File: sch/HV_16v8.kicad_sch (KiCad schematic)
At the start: 14 parts, among them J5 STPR_OUT, J6 Conn_01x03_Socket, U7 DRV8461SPWP

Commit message: gah
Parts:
- C30: footprint Capacitor_SMD:CP_Elec_8x10 -> Capacitor_THT:CP_Radial_D8.0mm_P3.50mm
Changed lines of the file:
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@@
 			)
 		)
-		(property "Footprint" "Capacitor_SMD:CP_Elec_8x10"
+		(property "Footprint" "Capacitor_THT:CP_Radial_D8.0mm_P3.50mm"
 			(at 20.0152 30.48 0)
 			(hide yes)

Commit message: reroute
doooom
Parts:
- added C46: 1uF, Capacitor_SMD:C_0402_1005Metric, symbol Device:C_Small
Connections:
- net BOUT1: now also J5.4 (Pin_4); no longer J5.3 (Pin_3)
- net BOUT2: now also J5.3 (Pin_3); no longer J5.4 (Pin_4)
- net DVDD: now also C46.1
- net GND: now also C46.2
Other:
- moved on the sheet: C34
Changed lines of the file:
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@@
+	)
+	(junction
+		(at 82.55 45.72)
+		(diameter 0)
+		(color 0 0 0 0)
+	)
+	(junction
+		(at 92.71 39.37)
+		(diameter 0)
+		(color 0 0 0 0)
+	)
+	(junction
+		(at 41.91 30.48)
+		(diameter 0)
+		(color 0 0 0 0)
+	)
+	(junction
+		(at 104.14 39.37)
+		(diameter 0)
+		(color 0 0 0 0)
+	)
+	(junction
+		(at 104.14 44.45)
+		(diameter 0)
+		(color 0 0 0 0)
+	)
+	(junction
+		(at 63.5 55.88)
+		(diameter 0)
+		(color 0 0 0 0)
 	)
 	(junction
@@
 	)
 	(junction
-		(at 82.55 45.72)
+		(at 30.48 30.48)
 		(diameter 0)
 		(color 0 0 0 0)
 	)
 	(junction
-		(at 92.71 39.37)
+		(at 115.57 44.45)
 		(diameter 0)
 		(color 0 0 0 0)
 	)
 	(junction
-		(at 41.91 30.48)
-		(diameter 0)
-		(color 0 0 0 0)
-	)
-	(junction
-		(at 104.14 39.37)
-		(diameter 0)
-		(color 0 0 0 0)
-	)
-	(junction
-		(at 104.14 44.45)
-		(diameter 0)
-		(color 0 0 0 0)
-	)
-	(junction
-		(at 63.5 55.88)
+		(at 115.57 39.37)
 		(diameter 0)
 		(color 0 0 0 0)
@@
 		(color 0 0 0 0)
 	)
-	(junction
-		(at 30.48 30.48)
-		(diameter 0)
-		(color 0 0 0 0)
-	)
-	(junction
-		(at 115.57 44.45)
-		(diameter 0)
-		(color 0 0 0 0)
-	)
-	(junction
-		(at 115.57 39.37)
-		(diameter 0)
-		(color 0 0 0 0)
-	)
 	(wire
 		(pts
@@
 	(wire
 		(pts
+			(xy 19.05 20.32) (xy 19.05 22.86)
+		)
+		(stroke
+			(width 0)
+			(type default)
+		)
+	)
+	(wire
+		(pts
 			(xy 41.91 30.48) (xy 41.91 33.02)
 		)
@@
 	(wire
 		(pts
+			(xy 55.88 83.82) (xy 55.88 88.9)
+		)
+		(stroke
+			(width 0)
+			(type default)
+		)
+	)
+	(wire
+		(pts
 			(xy 64.77 83.82) (xy 69.85 83.82)
 		)
@@
 	)
 	(label "BOUT2"
-		(at 142.24 69.85 180)
+		(at 142.24 67.31 180)
 		(effects
 			(font
@@
 	)
 	(label "BOUT1"
-		(at 142.24 67.31 180)
+		(at 142.24 69.85 180)
 		(effects
 			(font
@@
 	(label "VM"
 		(at 113.03 60.96 180)
+		(effects
+			(font
+				(size 1.27 1.27)
+			)
+			(justify right bottom)
+		)
+	)
+	(label "DVDD"
+		(at 35.56 52.07 180)
 		(effects
 			(font
@@
 	(symbol
 		(lib_id "Device:C_Small")
+		(at 35.56 54.61 0)
+		(mirror y)
+		(unit 1)
+		(body_style 1)
+		(exclude_from_sim no)
+		(in_bom yes)
+		(on_board yes)
+		(in_pos_files yes)
+		(dnp no)
+		(property "Reference" "C46"
+			(at 33.02 53.3462 0)
+			(show_name no)
+			(do_not_autoplace no)
+			(effects
+				(font
+					(size 1.27 1.27)
+				)
+				(justify left)
+			)
+		)
+		(property "Value" "1uF"
+			(at 33.02 55.8862 0)
+			(show_name no)
+			(do_not_autoplace no)
+			(effects
+				(font
+					(size 1.27 1.27)
+				)
+				(justify left)
+			)
+		)
+		(property "Footprint" "Capacitor_SMD:C_0402_1005Metric"
+			(at 35.56 54.61 0)
+			(hide yes)
+			(show_name no)
+			(do_not_autoplace no)
+			(effects
+				(font
+					(size 1.27 1.27)
+				)
+			)
+		)
+		(property "Datasheet" ""
+			(at 35.56 54.61 0)
+			(hide yes)
+			(show_name no)
+			(do_not_autoplace no)
+			(effects
+				(font
+					(size 1.27 1.27)
+				)
+			)
+		)
+		(property "Description" "Unpolarized capacitor, small symbol"
+			(at 35.56 54.61 0)
+			(hide yes)
+			(show_name no)
+			(do_not_autoplace no)
+			(effects
+				(font
+					(size 1.27 1.27)
+				)
+			)
+		)
+		(pin "2"
+		)
+		(pin "1"
+		)
+		(instances
+			(project "rp2354b-fast"
+				(path "/beb1ad91-9446-4312-87f0-5238465df71d/0c7a7e89-d1ec-4229-95b4-103dc8c8523c"
+					(reference "C46")
+					(unit 1)
+				)
+			)
+		)
+	)
+	(symbol
+		(lib_id "Device:C_Small")
 		(at 58.42 58.42 0)
 		(mirror y)
@@
 	(symbol
 		(lib_id "power:GND")
-		(at 55.88 88.9 0)
+		(at 55.88 93.98 0)
 		(unit 1)
 		(body_style 1)
@@
 		(fields_autoplaced yes)
 		(property "Reference" "#PWR041"
-			(at 55.88 95.25 0)
+			(at 55.88 100.33 0)
 			(hide yes)
 			(show_name no)
@@
 		)
 		(property "Value" "GND"
+			(at 55.88 99.06 0)
+			(show_name no)
+			(do_not_autoplace no)
+			(effects
+				(font
+					(size 1.27 1.27)
+				)
+			)
+		)
+		(property "Footprint" ""
 			(at 55.88 93.98 0)
-			(show_name no)
-			(do_not_autoplace no)
-			(effects
-				(font
-					(size 1.27 1.27)
-				)
-			)
-		)
-		(property "Footprint" ""
-			(at 55.88 88.9 0)
 			(hide yes)
 			(show_name no)
@@
 		)
 		(property "Datasheet" ""
-			(at 55.88 88.9 0)
+			(at 55.88 93.98 0)
 			(hide yes)
 			(show_name no)
@@
 		)
 		(property "Description" "Power symbol creates a global label with name \"GND\" , ground"
-			(at 55.88 88.9 0)
+			(at 55.88 93.98 0)
 			(hide yes)
 			(show_name no)
@@
 	(symbol
 		(lib_id "power:+BATT")
-		(at 19.05 22.86 0)
+		(at 19.05 20.32 0)
 		(mirror y)
 		(unit 1)
@@
 		(dnp no)
 		(property "Reference" "#PWR036"
-			(at 19.05 26.67 0)
+			(at 19.05 24.13 0)
 			(hide yes)
 			(show_name no)
@@
 		)
 		(property "Value" "+16V8"
-			(at 19.05 17.78 0)
+			(at 19.05 15.24 0)
 			(show_name no)
 			(do_not_autoplace no)
@@
 		)
 		(property "Footprint" ""
-			(at 19.05 22.86 0)
+			(at 19.05 20.32 0)
 			(hide yes)
 			(show_name no)
@@
 		)
 		(property "Datasheet" ""
-			(at 19.05 22.86 0)
+			(at 19.05 20.32 0)
 			(hide yes)
 			(show_name no)
@@
 		)
 		(property "Description" "Power symbol creates a global label with name \"+BATT\""
-			(at 19.05 22.86 0)
+			(at 19.05 20.32 0)
 			(hide yes)
 			(show_name no)
@@
 				(path "/beb1ad91-9446-4312-87f0-5238465df71d/0c7a7e89-d1ec-4229-95b4-103dc8c8523c"
 					(reference "C31")
+					(unit 1)
+				)
+			)
+		)
+	)
+	(symbol
+		(lib_id "power:GND")
+		(at 35.56 57.15 0)
+		(unit 1)
+		(body_style 1)
+		(exclude_from_sim no)
+		(in_bom yes)
+		(on_board yes)
+		(in_pos_files yes)
+		(dnp no)
+		(fields_autoplaced yes)
+		(property "Reference" "#PWR070"
+			(at 35.56 63.5 0)
+			(hide yes)
+			(show_name no)
+			(do_not_autoplace no)
+			(effects
+				(font
+					(size 1.27 1.27)
+				)
+			)
+		)
+		(property "Value" "GND"
+			(at 35.56 62.23 0)
+			(show_name no)
+			(do_not_autoplace no)
+			(effects
+				(font
+					(size 1.27 1.27)
+				)
+			)
+		)
+		(property "Footprint" ""
+			(at 35.56 57.15 0)
+			(hide yes)
+			(show_name no)
+			(do_not_autoplace no)
+			(effects
+				(font
+					(size 1.27 1.27)
+				)
+			)
+		)
+		(property "Datasheet" ""
+			(at 35.56 57.15 0)
+			(hide yes)
+			(show_name no)
+			(do_not_autoplace no)
+			(effects
+				(font
+					(size 1.27 1.27)
+				)
+			)
+		)
+		(property "Description" "Power symbol creates a global label with name \"GND\" , ground"
+			(at 35.56 57.15 0)
+			(hide yes)
+			(show_name no)
+			(do_not_autoplace no)
+			(effects
+				(font
+					(size 1.27 1.27)
+				)
+			)
+		)
+		(pin "1"
+		)
+		(instances
+			(project "rp2354b-fast"
+				(path "/beb1ad91-9446-4312-87f0-5238465df71d/0c7a7e89-d1ec-4229-95b4-103dc8c8523c"
+					(reference "#PWR070")
 					(unit 1)
 				)
@@
 	(symbol
 		(lib_id "Device:C_Small")
-		(at 55.88 86.36 0)
+		(at 55.88 91.44 0)
 		(mirror y)
 		(unit 1)
@@
 		(dnp no)
 		(property "Reference" "C34"
-			(at 53.34 85.0962 0)
+			(at 53.34 90.1762 0)
 			(show_name no)
 			(do_not_autoplace no)
@@
 		)
 		(property "Value" "1uF"
-			(at 53.34 87.6362 0)
+			(at 53.34 92.7162 0)
 			(show_name no)
 			(do_not_autoplace no)
@@
 		)
 		(property "Footprint" "Capacitor_SMD:C_0402_1005Metric"
-			(at 55.88 86.36 0)
+			(at 55.88 91.44 0)
 			(hide yes)
 			(show_name no)
@@
 		)
 		(property "Datasheet" ""
-			(at 55.88 86.36 0)
+			(at 55.88 91.44 0)
 			(hide yes)
 			(show_name no)
@@
 		)
 		(property "Description" "Unpolarized capacitor, small symbol"
-			(at 55.88 86.36 0)
-			(hide yes)
-			(show_name no)
+			(at 55.88 91.44 0)
+			(hide yes)
+			(show_name no)

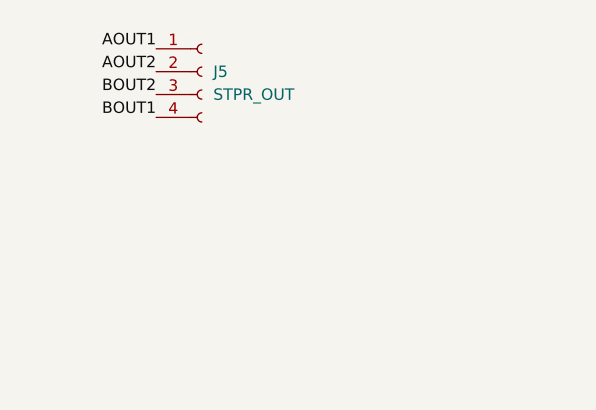
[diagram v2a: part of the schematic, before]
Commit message: v1.1e
added header pins for the driver and some extras for rbf and others.
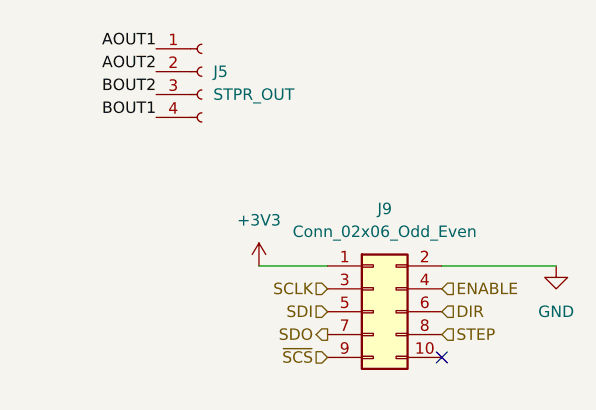
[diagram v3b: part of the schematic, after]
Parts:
- added J9: Conn_02x06_Odd_Even, Connector_PinHeader_2.54mm:PinHeader_2x05_P2.54mm_Vertical, symbol Connector_Generic:Conn_02x05_Odd_Even
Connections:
- net +3V3: now also J9.1 (Pin_1)
- net DIR: now also J9.6 (Pin_6)
- net ENABLE: now also J9.4 (Pin_4)
- net GND: now also J9.2 (Pin_2)
- net SCLK: now also J9.3 (Pin_3)
- net SDI: now also J9.5 (Pin_5)
- net SDO: now also J9.7 (Pin_7)
- net STEP: now also J9.8 (Pin_8)
- net ~{SCS}: now also J9.9 (Pin_9)
- no-connect marks 0 -> 1

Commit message: v1.1e for real
ordered!
Redid high power side.
Added breakouts for power and the motor driver.
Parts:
- removed J6: Conn_01x03_Socket, Connector_AMASS:AMASS_XT60IPW-M_1x03_P7.20mm_Horizontal, symbol Connector:Conn_01x03_Socket
- added J8: Conn_01x02_Socket, Connector_AMASS:AMASS_XT30PW-M_1x02_P2.50mm_Horizontal, symbol Connector:Conn_01x02_Socket
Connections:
- net GND: now also J8.2 (Pin_2)
- net at D4.1: now also J8.1 (Pin_1)
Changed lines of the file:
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@@
-	)
-	(junction
-		(at 41.91 30.48)
-		(diameter 0)
-		(color 0 0 0 0)
 	)
 	(junction
@@
 		(pts
 			(xy 19.05 20.32) (xy 19.05 22.86)
-		)
-		(stroke
-			(width 0)
-			(type default)
-		)
-	)
-	(wire
-		(pts
-			(xy 41.91 30.48) (xy 41.91 33.02)
 		)
 		(stroke
@@
 	)
 	(symbol
+		(lib_id "Connector:Conn_01x02_Socket")
+		(at 46.99 27.94 0)
+		(unit 1)
+		(body_style 1)
+		(exclude_from_sim no)
+		(in_bom yes)
+		(on_board yes)
+		(in_pos_files yes)
+		(dnp no)
+		(fields_autoplaced yes)
+		(property "Reference" "J8"
+			(at 48.26 27.9399 0)
+			(show_name no)
+			(do_not_autoplace no)
+			(effects
+				(font
+					(size 1.27 1.27)
+				)
+				(justify left)
+			)
+		)
+		(property "Value" "Conn_01x02_Socket"
+			(at 48.26 30.4799 0)
+			(show_name no)
+			(do_not_autoplace no)
+			(effects
+				(font
+					(size 1.27 1.27)
+				)
+				(justify left)
+			)
+		)
+		(property "Footprint" "Connector_AMASS:AMASS_XT30PW-M_1x02_P2.50mm_Horizontal"
+			(at 46.99 27.94 0)
+			(hide yes)
+			(show_name no)
+			(do_not_autoplace no)
+			(effects
+				(font
+					(size 1.27 1.27)
+				)
+			)
+		)
+		(property "Datasheet" ""
+			(at 46.99 27.94 0)
+			(hide yes)
+			(show_name no)
+			(do_not_autoplace no)
+			(effects
+				(font
+					(size 1.27 1.27)
+				)
+			)
+		)
+		(property "Description" "Generic connector, single row, 01x02, script generated"
+			(at 46.99 27.94 0)
+			(hide yes)
+			(show_name no)
+			(do_not_autoplace no)
+			(effects
+				(font
+					(size 1.27 1.27)
+				)
+			)
+		)
+		(pin "1"
+		)
+		(pin "2"
+		)
+		(instances
+			(project "rp2354b-fast"
+				(path "/beb1ad91-9446-4312-87f0-5238465df71d/0c7a7e89-d1ec-4229-95b4-103dc8c8523c"
+					(reference "J8")
+					(unit 1)
+				)
+			)
+		)
+	)
+	(symbol
 		(lib_id "Device:C")
 		(at 19.05 26.67 0)
@@
 					(unit 1)
 				)
-			)
-		)
-	)
-	(symbol
-		(lib_id "Connector:Conn_01x03_Socket")
-		(at 46.99 30.48 0)
-		(unit 1)
-		(body_style 1)
-		(exclude_from_sim no)
-		(in_bom yes)
-		(on_board yes)
-		(in_pos_files yes)
-		(dnp no)
-		(fields_autoplaced yes)
-		(property "Reference" "J6"
-			(at 48.26 29.2099 0)
-			(show_name no)
-			(do_not_autoplace no)
-			(effects
-				(font
-					(size 1.27 1.27)
-				)
-				(justify left)
-			)
-		)
-		(property "Value" "Conn_01x03_Socket"
-			(at 48.26 31.7499 0)
-			(show_name no)
-			(do_not_autoplace no)
-			(effects
-				(font
-					(size 1.27 1.27)
-				)
-				(justify left)
-			)
-		)
-		(property "Footprint" "Connector_AMASS:AMASS_XT60IPW-M_1x03_P7.20mm_Horizontal"
-			(at 46.99 30.48 0)
-			(hide yes)
-			(show_name no)
-			(do_not_autoplace no)
-			(effects
-				(font
-					(size 1.27 1.27)
-				)
-			)
-		)
-		(property "Datasheet" ""
-			(at 46.99 30.48 0)
-			(hide yes)
-			(show_name no)
-			(do_not_autoplace no)
-			(effects
-				(font
-					(size 1.27 1.27)
-				)
-			)
-		)
-		(property "Description" "Generic connector, single row, 01x03, script generated"
-			(at 46.99 30.48 0)
-			(hide yes)
-			(show_name no)
-			(do_not_autoplace no)
-			(effects
-				(font
-					(size 1.27 1.27)
-				)
-			)
-		)
-		(pin "3"
-		)
-		(pin "1"
-		)
-		(pin "2"
-		)
-		(instances
-			(project "rp2354b-fast"
-				(path "/beb1ad91-9446-4312-87f0-5238465df71d/0c7a7e89-d1ec-4229-95b4-103dc8c8523c"
-					(reference "J6")
-					(unit 1)
-				)
